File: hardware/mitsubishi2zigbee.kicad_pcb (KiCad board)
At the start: 2 copper layers, 30 x 45 mm, 10 parts, among them J1 CN105, Q1 BSS138, Q2 BSS138, U1 ESP32-C6-Zero

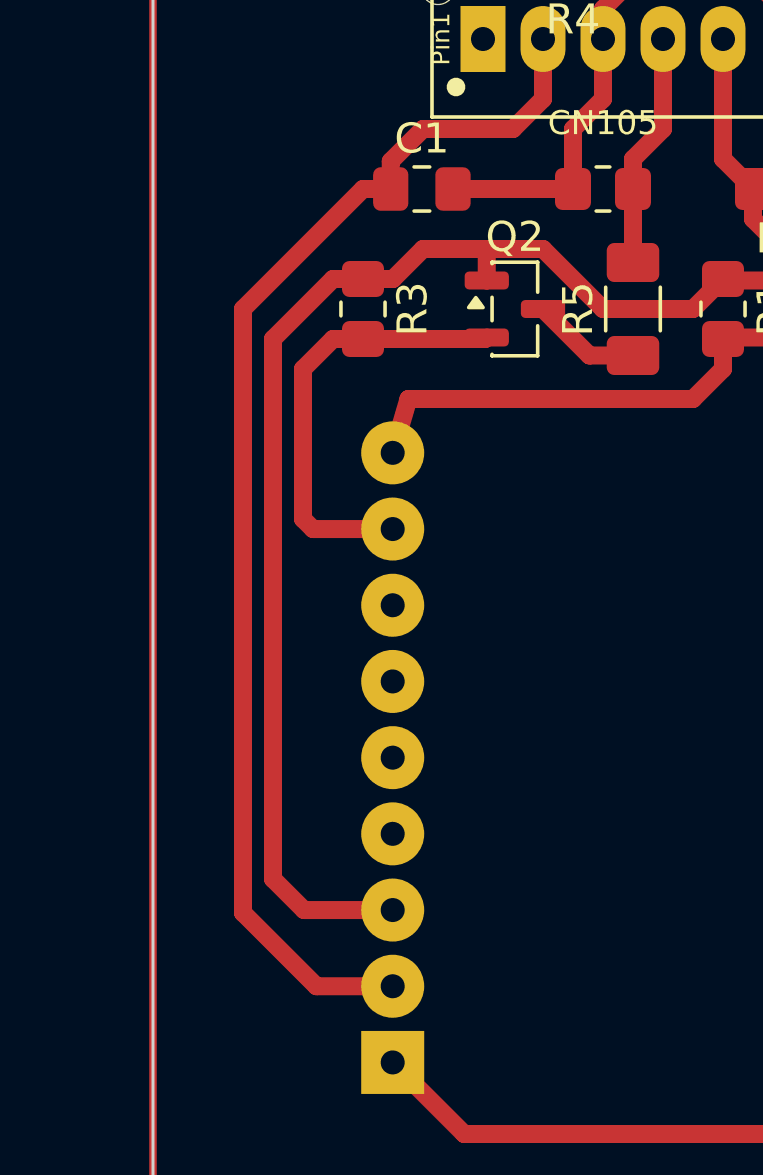
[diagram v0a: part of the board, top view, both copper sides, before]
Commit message: fix(pcb): increase clearance between left-side parallel tracks to 0.9mm
- Shift GND track outward to x=113.6mm and /TX_3V3 inward to x=116.4mm
- Set track widths to 0.5mm on the parallel bus (+3V3, GND, /TX_3V3)
- Expand inter-track clearance from 0.4mm to 0.9mm (well above the 0.4mm etching minimum)
- Maintain strict 45-degree routing and 0 DRC/connectivity errors
- Regenerate etching typons (typon_echelle1_A4.pdf and typon_echelle1_carte.svg)
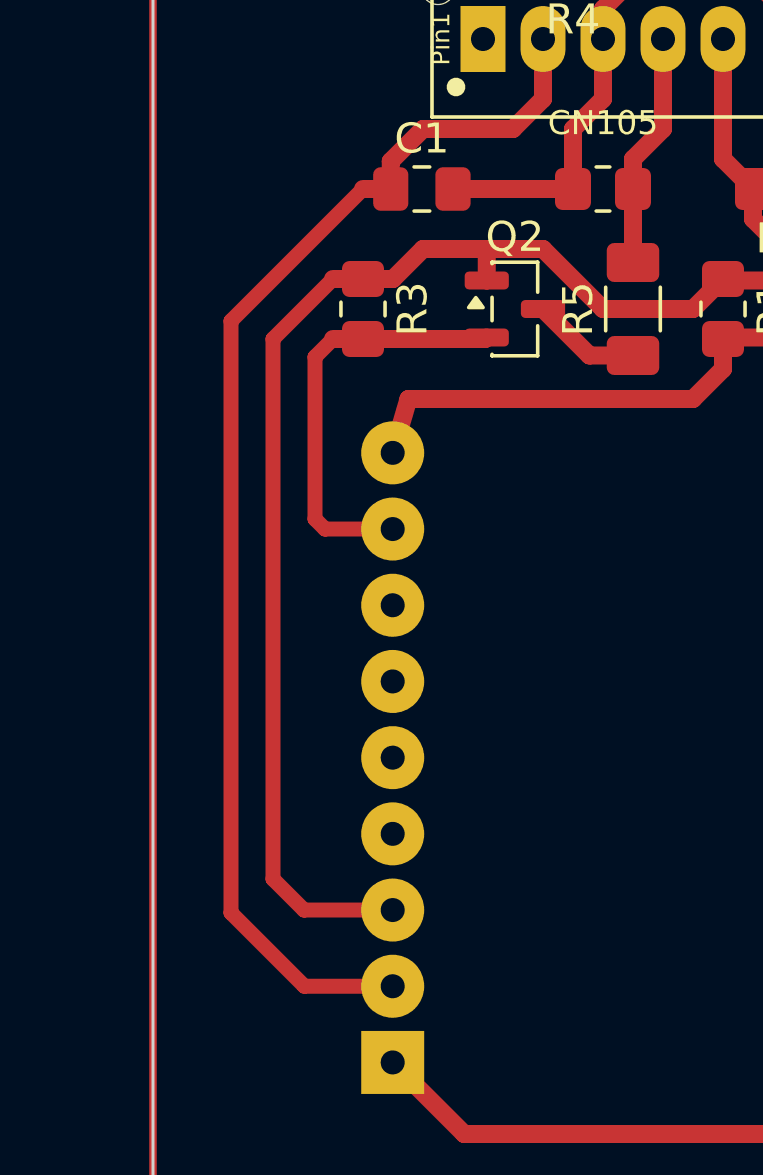
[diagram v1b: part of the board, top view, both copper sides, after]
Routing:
- net /TX_3V3: track 14.7 -> 14.1 mm
- net GND: track 41.6 -> 42.2 mm
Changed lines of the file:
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@@
 		(start 118.99 65.035)
 		(end 116.035 65.035)
-		(width 0.6)
+		(width 0.5)
 		(layer "F.Cu")
 		(net "+3V3")
@@
 		(start 116.035 65.035)
 		(end 115 64)
-		(width 0.6)
+		(width 0.5)
 		(layer "F.Cu")
 		(net "+3V3")
@@
 		(start 115 64)
 		(end 115 46)
-		(width 0.6)
+		(width 0.5)
 		(layer "F.Cu")
 		(net "+3V3")
@@
 		(start 115 46)
 		(end 117 44)
-		(width 0.6)
+		(width 0.5)
 		(layer "F.Cu")
 		(net "+3V3")
@@
 	)
 	(segment
-		(start 116.335 52.335)
-		(end 116 52)
-		(width 0.6)
+		(start 116.735 52.335)
+		(end 116.4 52)
+		(width 0.5)
 		(layer "F.Cu")
 		(net "/TX_3V3")
@@
 	(segment
 		(start 117 46)
-		(end 116 47)
-		(width 0.6)
+		(end 116.4 46.6)
+		(width 0.5)
 		(layer "F.Cu")
 		(net "/TX_3V3")
@@
 	(segment
 		(start 118.99 52.335)
-		(end 116.335 52.335)
-		(width 0.6)
+		(end 116.735 52.335)
+		(width 0.5)
 		(layer "F.Cu")
 		(net "/TX_3V3")
@@
 	)
 	(segment
-		(start 116 52)
-		(end 116 47)
-		(width 0.6)
+		(start 116.4 52)
+		(end 116.4 46.6)
+		(width 0.5)
 		(layer "F.Cu")
 		(net "/TX_3V3")
@@
 	)
 	(segment
-		(start 114 65.127792)
-		(end 114 45)
-		(width 0.6)
+		(start 113.6 65.127792)
+		(end 113.6 45.4)
+		(width 0.5)
 		(layer "F.Cu")
 		(net "GND")
@@
 	(segment
 		(start 118.99 67.575)
-		(end 116.447208 67.575)
-		(width 0.6)
-		(layer "F.Cu")
-		(net "GND")
-	)
-	(segment
-		(start 116.447208 67.575)
-		(end 114 65.127792)
-		(width 0.6)
+		(end 116.047208 67.575)
+		(width 0.5)
+		(layer "F.Cu")
+		(net "GND")
+	)
+	(segment
+		(start 116.047208 67.575)
+		(end 113.6 65.127792)
+		(width 0.5)
 		(layer "F.Cu")
 		(net "GND")
@@
 	)
 	(segment
-		(start 114 45)
+		(start 113.6 45.4)
 		(end 118 41)
-		(width 0.6)
-		(layer "F.Cu")
-		(net "GND")
+		(width 0.5)
+		(layer "F.Cu")
+		(net "GND")

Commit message: feat: Zigbee HVAC gateway with vane control and CN105 integration
Firmware and Z2M converter for full climate control (modes, setpoint, fan,
vane via cluster 0xFF00), corrected CN105 UART pins, and stripped debug/dead code.
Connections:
- J1 pad 4: /TX_5V -> /RX_5V
- J1 pad 5: /RX_5V -> /TX_5V
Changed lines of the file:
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@@
 			(layers "*.Cu" "*.Mask")
 			(remove_unused_layers no)
-			(net "/TX_5V")
+			(net "/RX_5V")
 			(pinfunction "Pin_4_4")
 			(pintype "passive")
@@
 			(layers "*.Cu" "*.Mask")
 			(remove_unused_layers no)
-			(net "/RX_5V")
+			(net "/TX_5V")
 			(pinfunction "Pin_5_5")
 			(pintype "passive")
